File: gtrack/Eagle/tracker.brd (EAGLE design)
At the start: 50.2 x 50 mm, 59 parts, among them IC1 STM32L152RBT, IC2 TPS73601, U2 SIM900, U3 MCP73831, X1 MINI-USB-32005-301

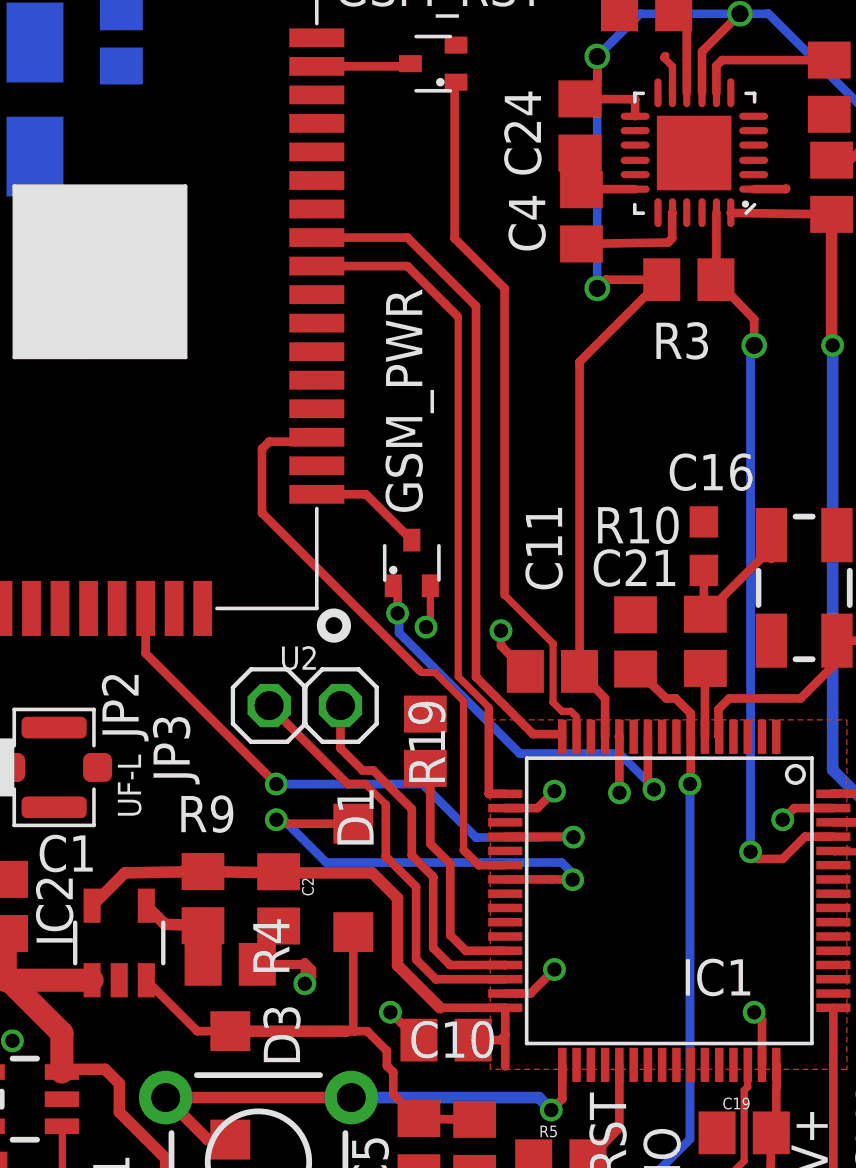
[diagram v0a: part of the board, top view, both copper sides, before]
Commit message: Increase pad distance
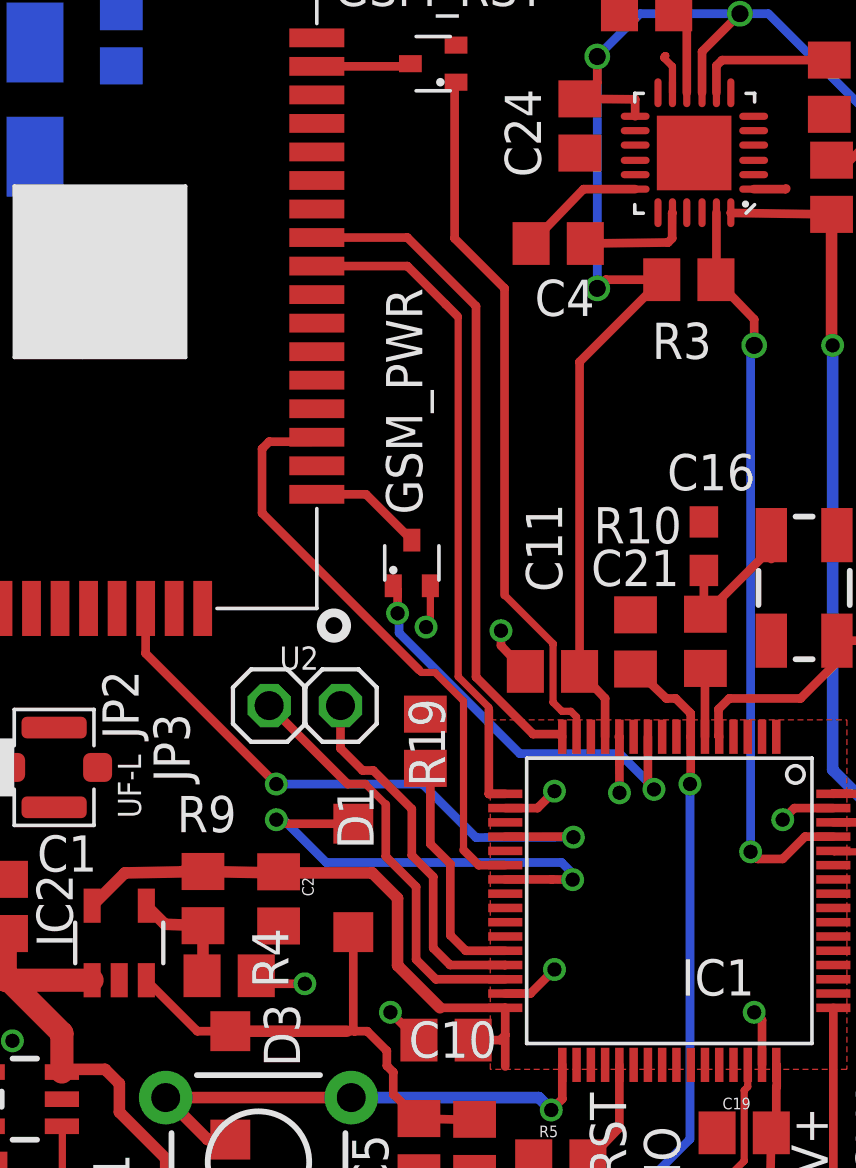
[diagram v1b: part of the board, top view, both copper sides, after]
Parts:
- moved C4 1.24 mm to (35.4, 36.4), turned to 180 degrees
- moved R4 0.40 mm to (23.8, 10.8)
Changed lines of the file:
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@@
 <attribute name="VALUE" x="39.74875" y="47.17375" size="1.27" layer="27" rot="R180"/>
 </element>
-<element name="C4" library="rcl" package="C0805" value="2.2n" x="36.19625" y="37.38125" smashed="yes" rot="R90">
-<attribute name="OC_NEWARK" value="unknown" x="36.19625" y="37.38125" size="1.778" layer="27" rot="R90" display="off"/>
-<attribute name="MF" value="" x="36.19625" y="37.38125" size="1.778" layer="27" rot="R90" display="off"/>
-<attribute name="MPN" value="" x="36.19625" y="37.38125" size="1.778" layer="27" rot="R90" display="off"/>
-<attribute name="NAME" x="34.92625" y="36.11125" size="1.27" layer="25" rot="R90"/>
-<attribute name="VALUE" x="38.73625" y="36.11125" size="1.27" layer="27" rot="R90"/>
+<element name="C4" library="rcl" package="C0805" value="2.2n" x="35.38125" y="36.44625" smashed="yes" rot="R180">
+<attribute name="OC_NEWARK" value="unknown" x="35.38125" y="36.44625" size="1.778" layer="27" rot="R180" display="off"/>
+<attribute name="MF" value="" x="35.38125" y="36.44625" size="1.778" layer="27" rot="R180" display="off"/>
+<attribute name="MPN" value="" x="35.38125" y="36.44625" size="1.778" layer="27" rot="R180" display="off"/>
+<attribute name="NAME" x="36.65125" y="35.17625" size="1.27" layer="25" rot="R180"/>
+<attribute name="VALUE" x="36.65125" y="38.98625" size="1.27" layer="27" rot="R180"/>
 </element>
 <element name="C8" library="rcl" package="C0805" value="22p" x="20.0675" y="43.62125" smashed="yes" rot="MR270">
@@
 <attribute name="VALUE" x="40.595" y="37.7175" size="1.27" layer="27" rot="R180"/>
 </element>
-<element name="R4" library="rcl" package="R0805" value="30.9k" x="23.885" y="11.18" smashed="yes">
-<attribute name="OC_NEWARK" value="unknown" x="23.885" y="11.18" size="1.778" layer="27" display="off"/>
-<attribute name="MF" value="" x="23.885" y="11.18" size="1.778" layer="27" display="off"/>
-<attribute name="MPN" value="" x="23.885" y="11.18" size="1.778" layer="27" display="off"/>
-<attribute name="NAME" x="25.9625" y="10.7625" size="1.27" layer="25" rot="R90"/>
-<attribute name="VALUE" x="23.25" y="8.64" size="1.27" layer="27"/>
+<element name="R4" library="rcl" package="R0805" value="30.9k" x="23.8475" y="10.78" smashed="yes">
+<attribute name="OC_NEWARK" value="unknown" x="23.8475" y="10.78" size="1.778" layer="27" display="off"/>
+<attribute name="MF" value="" x="23.8475" y="10.78" size="1.778" layer="27" display="off"/>
+<attribute name="MPN" value="" x="23.8475" y="10.78" size="1.778" layer="27" display="off"/>
+<attribute name="NAME" x="25.925" y="10.3625" size="1.27" layer="25" rot="R90"/>
+<attribute name="VALUE" x="23.2125" y="8.24" size="1.27" layer="27"/>
 </element>
 <element name="R9" library="rcl" package="R0805" value="46.4k" x="22.93" y="13.485" smashed="yes" rot="R270">
@@
 <wire x1="43.657" y1="16.657" x2="43.25" y2="16.25" width="0.3048" layer="1"/>
 <via x="43.25" y="16.25" extent="1-16" drill="0.5"/>
-<wire x1="24.835" y1="11.18" x2="26.57" y2="11.18" width="0.3048" layer="1"/>
-<wire x1="26.57" y1="11.18" x2="26.75" y2="11" width="0.3048" layer="1"/>
-<wire x1="26.75" y1="11" x2="26.75" y2="10.75" width="0.3048" layer="1"/>
-<wire x1="26.75" y1="10.75" x2="26.5" y2="10.5" width="0.3048" layer="1"/>
-<wire x1="24.835" y1="11.18" x2="26.43" y2="11.18" width="0.3048" layer="1"/>
-<wire x1="26.43" y1="11.18" x2="26.5" y2="11.25" width="0.3048" layer="1"/>
-<wire x1="26.5" y1="11.25" x2="26.5" y2="10.5" width="0.3048" layer="1"/>
 <via x="26.5" y="10.5" extent="1-16" drill="0.5"/>
 <wire x1="30.5" y1="8.525" x2="30.475" y2="8.525" width="0.3048" layer="1"/>
@@
 <via x="29.5" y="9.5" extent="1-16" drill="0.5"/>
 <wire x1="38.0788" y1="38.35205" x2="36.26705" y2="38.35205" width="0.3048" layer="1"/>
-<wire x1="36.26705" y1="38.35205" x2="36.19625" y2="38.33125" width="0.3048" layer="1"/>
+<wire x1="36.26705" y1="38.35205" x2="34.43125" y2="36.44625" width="0.3048" layer="1"/>
 <wire x1="42.2312" y1="38.35205" x2="43.35205" y2="38.35205" width="0.3048" layer="1"/>
 <wire x1="43.35205" y1="38.35205" x2="43.375" y2="38.375" width="0.3048" layer="1"/>
@@
 <wire x1="39.1375" y1="43.025" x2="39.125" y2="43.0125" width="0.254" layer="1"/>
 <wire x1="39.125" y1="43.0125" x2="39.1" y2="43.0125" width="0.254" layer="1"/>
+<wire x1="26.5" y1="10.5" x2="24.7975" y2="10.5" width="0.3048" layer="1"/>
+<wire x1="24.7975" y1="10.5" x2="24.7975" y2="10.78" width="0.3048" layer="1"/>
 </signal>
 <signal name="SIM_DATA">
@@
 <wire x1="22.9" y1="12.555" x2="22.93" y2="12.535" width="0.4064" layer="1"/>
 <wire x1="22.93" y1="12.535" x2="22.93" y2="11.235" width="0.4064" layer="1"/>
-<wire x1="22.93" y1="11.235" x2="22.935" y2="11.18" width="0.4064" layer="1"/>
+<wire x1="22.93" y1="11.235" x2="22.8975" y2="10.78" width="0.4064" layer="1"/>
 <wire x1="20.945" y1="13.236" x2="21.596" y2="12.585" width="0.4064" layer="1"/>
 <wire x1="21.596" y1="12.585" x2="22.93" y2="12.535" width="0.4064" layer="1"/>
@@
 <contactref element="MPU6050" pad="20"/>
 <contactref element="C4" pad="1"/>
-<wire x1="36.19625" y1="36.43125" x2="39.23125" y2="36.48125" width="0.3048" layer="1"/>
+<wire x1="36.33125" y1="36.44625" x2="39.23125" y2="36.48125" width="0.3048" layer="1"/>
 <wire x1="39.23125" y1="36.48125" x2="39.375" y2="36.625" width="0.3048" layer="1"/>
 <wire x1="39.375" y1="36.625" x2="39.375" y2="37.51675" width="0.3048" layer="1"/>

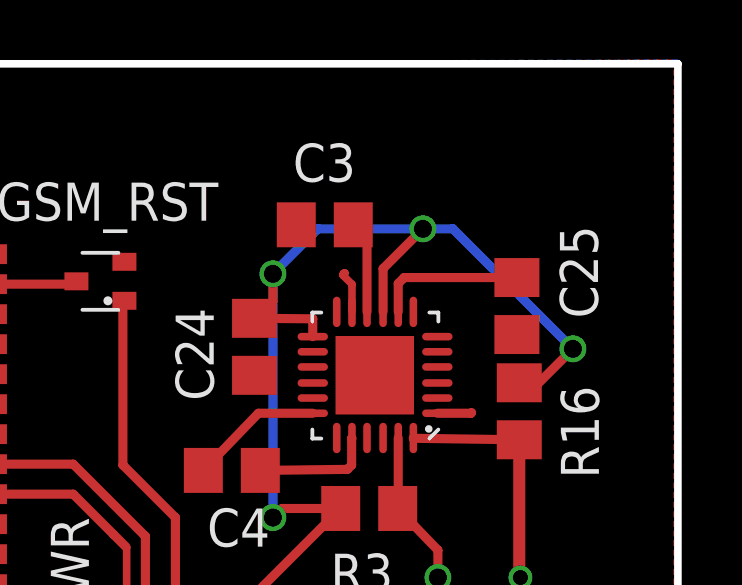
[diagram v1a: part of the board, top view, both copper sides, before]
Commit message: Fixed issue with missing MPU6050 power trace
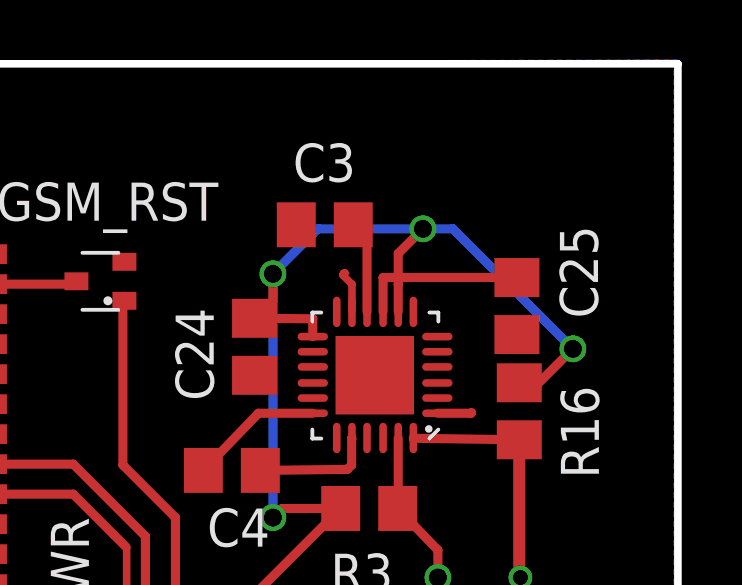
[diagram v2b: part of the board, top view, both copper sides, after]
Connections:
- removed net VIO: C25.1, MPU6050.8
- net V+: now also C25.1, MPU6050.8
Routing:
- net V+: track 80.8 -> 86.2 mm
- net VIO: track 4.99 -> 0.00 mm
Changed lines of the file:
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@@
 <wire x1="46.843" y1="16.157" x2="45.025" y2="16.157" width="0.3048" layer="1"/>
-</signal>
-<signal name="VIO">
-<contactref element="MPU6050" pad="8"/>
-<contactref element="C25" pad="1"/>
-<wire x1="40.9271" y1="41.73035" x2="40.9271" y2="42.6771" width="0.3048" layer="1"/>
-<wire x1="40.9271" y1="42.6771" x2="41.125" y2="42.875" width="0.3048" layer="1"/>
-<wire x1="41.125" y1="42.875" x2="44.83375" y2="42.875" width="0.3048" layer="1"/>
-<wire x1="44.83375" y1="42.875" x2="44.88375" y2="42.875" width="0.3048" layer="1"/>
 </signal>
 <signal name="VCC_GSM">
@@
 <wire x1="46.75" y1="40.5" x2="42.75" y2="44.5" width="0.3048" layer="16"/>
 <wire x1="42.75" y1="44.5" x2="41.75" y2="44.5" width="0.3048" layer="16"/>
-<wire x1="40.4225" y1="41.73035" x2="40.4225" y2="43.1725" width="0.3048" layer="1"/>
-<wire x1="40.4225" y1="43.1725" x2="41.75" y2="44.5" width="0.3048" layer="1"/>
 <wire x1="36.13" y1="21.4475" x2="36.13" y2="32.2975" width="0.3048" layer="1"/>
 <wire x1="36.13" y1="32.2975" x2="39.01" y2="35.1775" width="0.3048" layer="1"/>
+<contactref element="MPU6050" pad="8"/>
+<contactref element="C25" pad="1"/>
+<wire x1="40.9271" y1="42.8771" x2="40.4225" y2="42.8771" width="0.3048" layer="1"/>
+<wire x1="40.9271" y1="41.73035" x2="40.9271" y2="42.65" width="0.3048" layer="1"/>
+<wire x1="40.9271" y1="42.65" x2="40.9271" y2="42.8771" width="0.3048" layer="1"/>
+<wire x1="44.88375" y1="42.875" x2="44.88165" y2="42.8771" width="0.3048" layer="1"/>
+<wire x1="44.88165" y1="42.8771" x2="40.9271" y2="42.8771" width="0.3048" layer="1"/>
+<wire x1="41.75" y1="44.5" x2="40.9271" y2="43.6771" width="0.3048" layer="1"/>
+<wire x1="40.9271" y1="43.6771" x2="40.9271" y2="42.8771" width="0.3048" layer="1"/>
+<wire x1="40.4225" y1="41.73035" x2="40.4225" y2="42.8771" width="0.3048" layer="1"/>
 </signal>
 <signal name="N$4">
